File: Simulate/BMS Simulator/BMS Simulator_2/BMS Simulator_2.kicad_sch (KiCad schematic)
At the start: 25 parts, among them J101 24, Q101 NPN, Q102 NPN, Q103 NMOS, Q104 NPN, Q105 NPN, Q106 NMOS, Q107 NMOS, Q108 NMOS

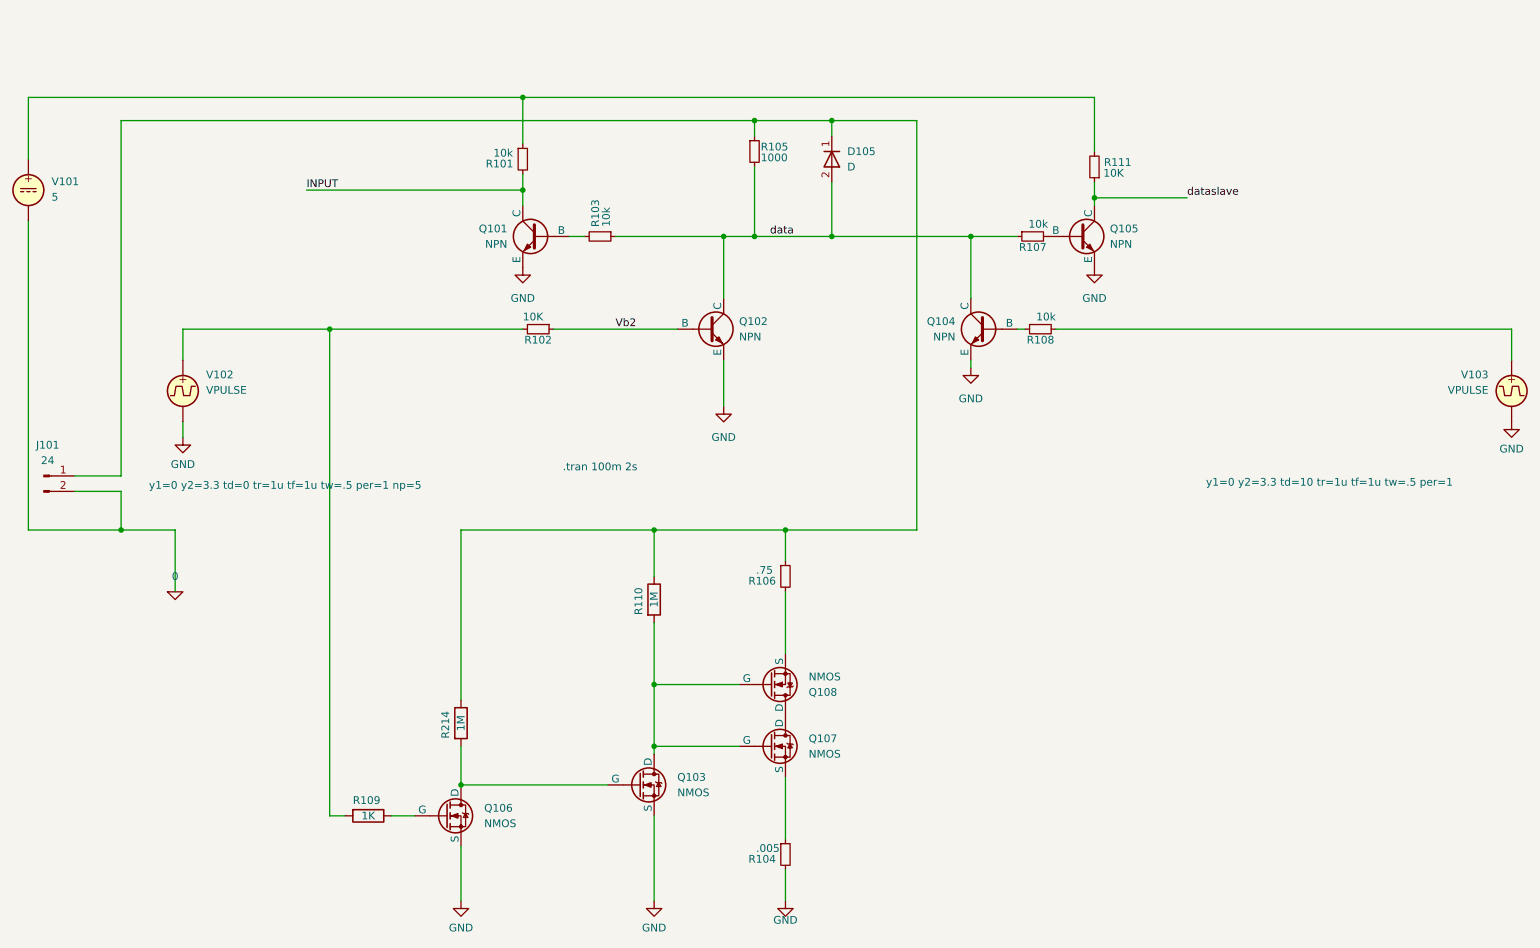
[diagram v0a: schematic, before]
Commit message: Simulation added bms Little improvements BMS Resistor divider added on the gate of the mosfet (Limmeded to +/-20V could be 30V during charging)
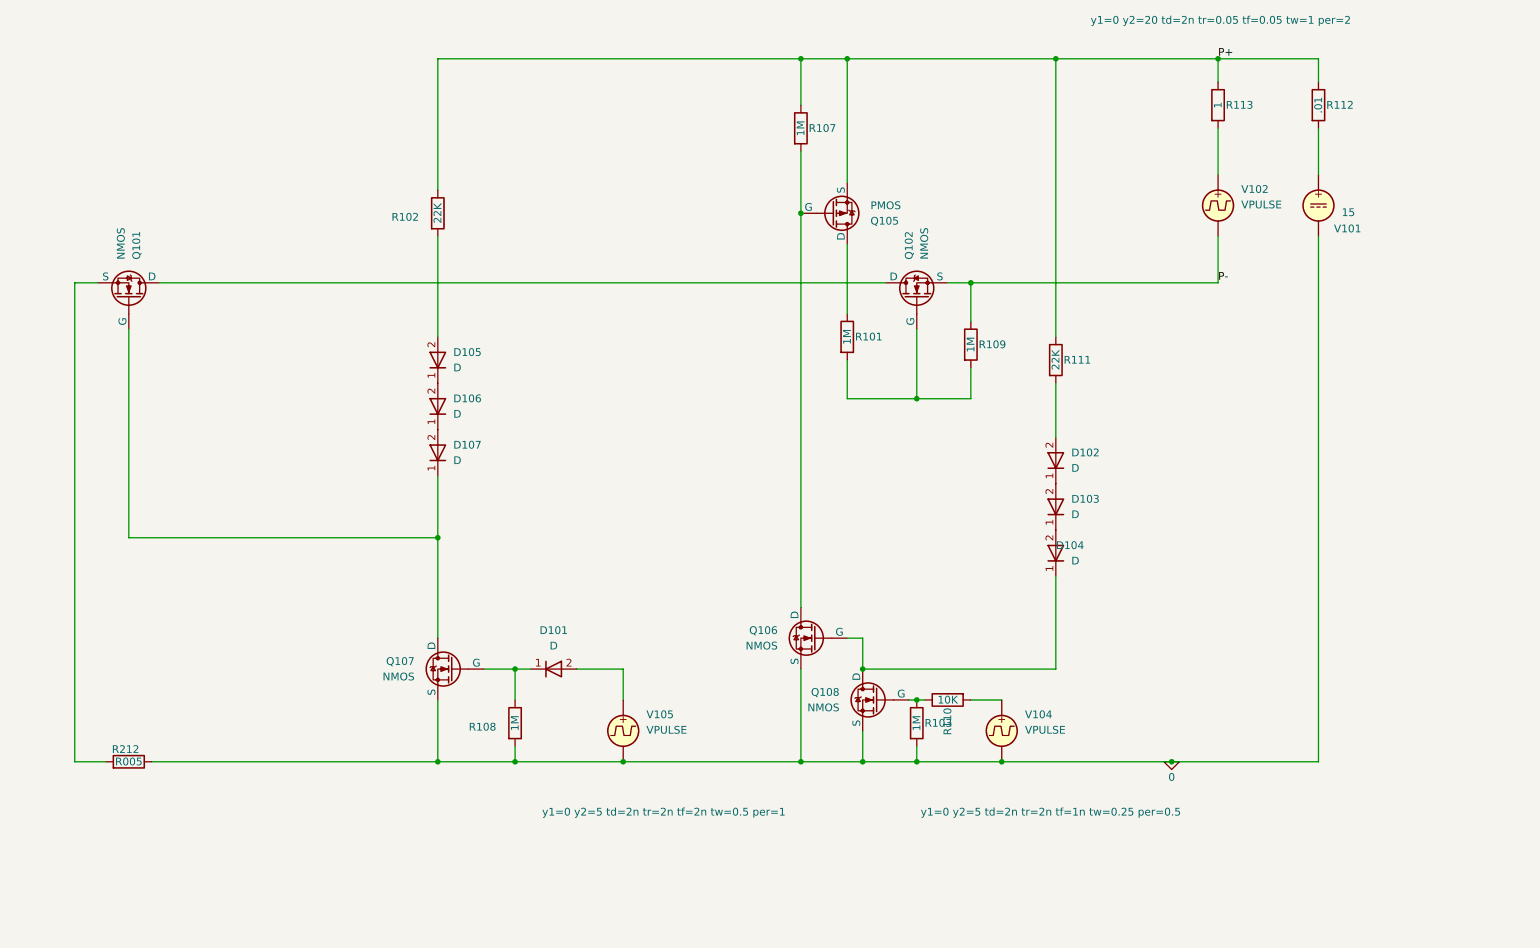
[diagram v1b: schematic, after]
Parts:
- removed J101: 24, symbol Connector:Conn_01x02_Pin
- removed Q101, Q102, Q104, Q105: NPN, symbol Simulation_SPICE:NPN
- removed Q103: NMOS, symbol Simulation_SPICE:NMOS
- removed R101, R103, R107, R108: 10k, A_Device:R_0603, symbol Device:R_Small
- removed R102, R111: 10K, A_Device:R_0603, symbol Device:R_Small
- removed R104: .005, A_Device:R_0603, symbol Device:R_Small
- removed R105: 1000, A_Device:R_0603, symbol Device:R_Small
- removed R106: .75, A_Device:R_0603, symbol Device:R_Small
- removed R214: 1M, A_Device:R_0603, symbol Device:R
- removed V103: VPULSE, symbol Simulation_SPICE:VPULSE
- added D101, D102, D103, D104, D106, D107: D, symbol Simulation_SPICE:D
- added Q101, Q102: NMOS, symbol Simulation_SPICE:NMOS
- added Q105: PMOS, symbol Simulation_SPICE:PMOS
- added R101, R103, R107, R108: 1M, A_Device:R_0603, symbol Device:R
- added R102, R111: 22K, A_Device:R_0603, symbol Device:R
- added R112: .01, A_Device:R_0603, symbol Device:R
- added R113: 1, A_Device:R_0603, symbol Device:R
- added R212: R005, Resistor_SMD:R_2512_6332Metric_Pad1.40x3.35mm_HandSolder, symbol Device:R
- added V104, V105: VPULSE, symbol Simulation_SPICE:VPULSE
- R109: value 1K -> 1M; LCSC (none) -> C22935
- R110: value 1M -> 10K; LCSC (none) -> C22935
- V101: value 5 -> 15
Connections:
- net 0: now also Q106.3 (S), Q107.3 (S), Q108.3 (S), R103.2, R108.2, R212.1, V104.2, V105.2
- net at V101.1: now also R112.2
- net at Q107.1 (D): now also D107.1 (K), Q101.2 (G); no longer Q108.1 (D)
- net at Q106.2 (G): now also Q108.1 (D), D104.1 (K); no longer R109.1
- net at R109.2: now also Q102.2 (G), R101.2; no longer V102.1
- net at Q106.1 (D): now also Q105.2 (G), R107.2
- net at R110.1: now also Q108.2 (G), R103.1; no longer D105.1 (K)
- net GND renamed P-
- net P-: now also R109.1, Q102.3 (S); no longer Q106.3 (S)
- net data: no longer names the net of D105.2 (A)
- net data: now also R102.2
- new net: Q105.1 (D), R101.1
- new net: D101.1 (K), Q107.2 (G), R108.1
- new net: D102.2 (A), R111.2
- new net: D102.1 (K), D103.2 (A)
- new net: D106.1 (K), D107.2 (A)
- new net: Q101.3 (S), R212.2
- new net: R110.2, V104.1
- new net: D101.2 (A), V105.1
- new net: R113.2, V102.1
- new net: D103.1 (K), D104.2 (A)
- new net: Q101.1 (D), Q102.1 (D)
- new net: D105.1 (K), D106.2 (A)
- new net P+: Q105.3 (S), R102.1, R107.1, R111.1, R112.1, R113.1
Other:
- note removed: ".tran 100m 2s"
